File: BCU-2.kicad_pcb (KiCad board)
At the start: 2 copper layers, 106 x 91.4 mm, 92 parts, among them J1 Screw_Terminal_01x04, J2 Conn_01x12_Male, J3 Screw_Terminal_01x04, J4 Conn_01x05_Male, J5 Conn_01x05_Male, J6 Conn_01x04_Male, J7 Conn_01x04_Male, Q1 2N7002, Q2 NTF6P02, Q3 2N7002, Q4 2N7002, Q5 NTF6P02, Q6 2N7002, U1 Teensy3.2, U10 74LV1T08, U11 74LV1T08, U12 INA219xID, U13 INA219xID, U2 HCPL-181, U3 HCPL-181, U4 HCPL-181, U5 HCPL-181, U6 HCPL-181, U7 HCPL-181, U8 74LV1T08, U9 74LV1T08

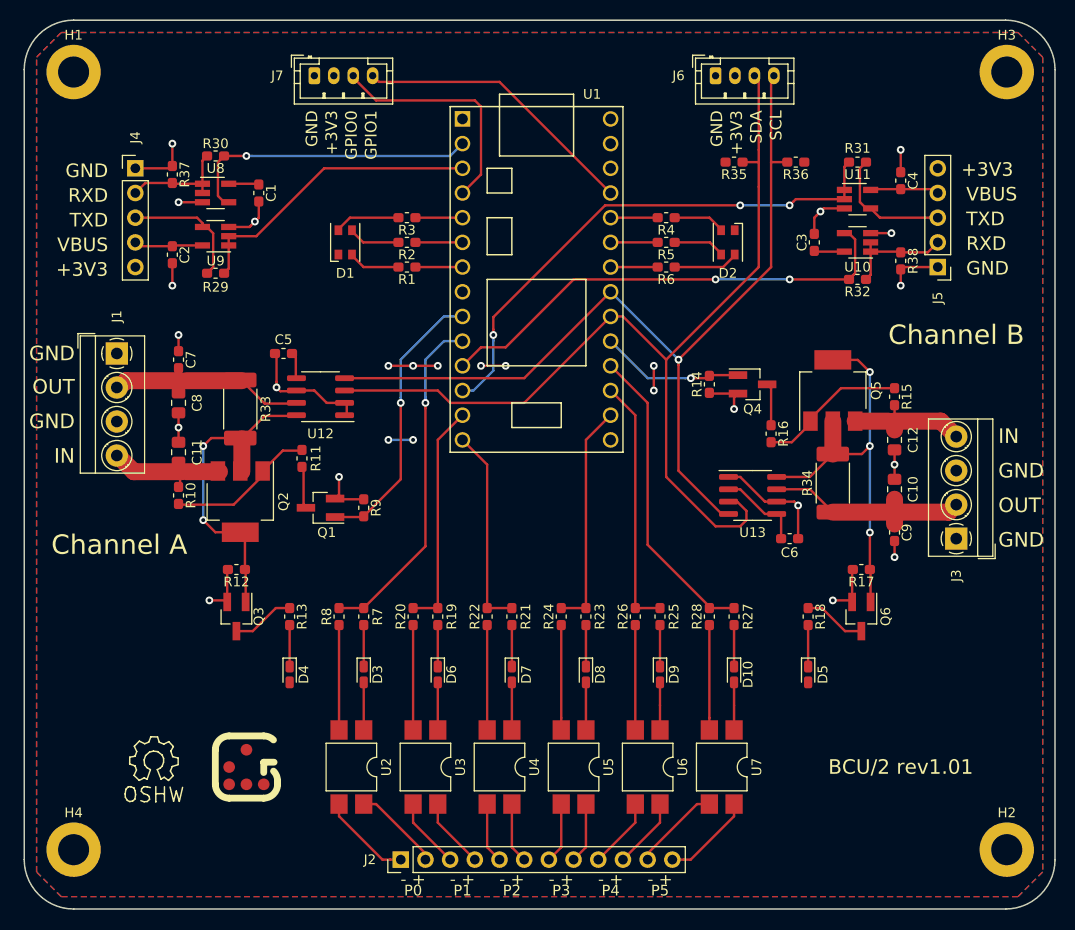
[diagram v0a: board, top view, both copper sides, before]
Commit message: PCB: Update layout for schematic changes
Signed-off-by: Geert Uytterhoeven <geert@linux-m68k.org>
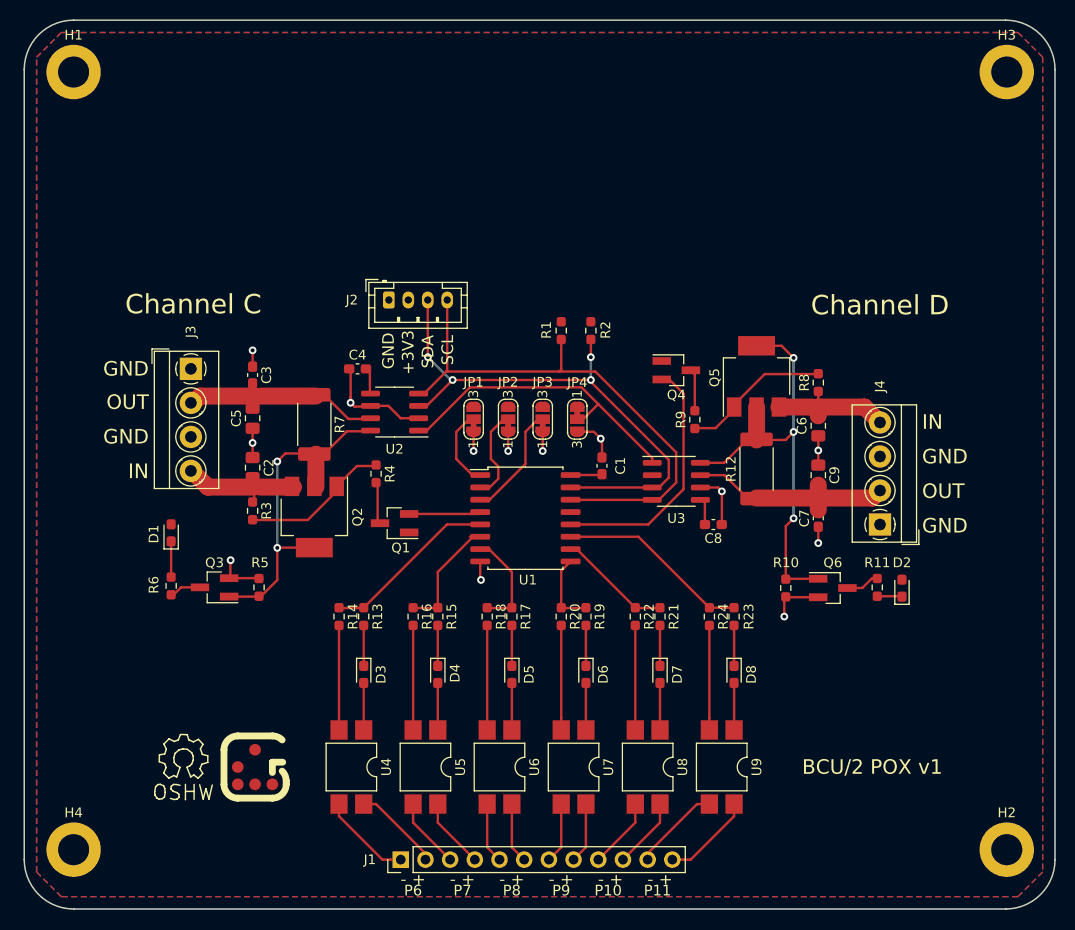
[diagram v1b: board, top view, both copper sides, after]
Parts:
- removed the C2 at (121.3, 66.7)
- removed the C3 at (187.3, 65.4)
- removed the C4 at (196.2, 59.1)
- removed the D1 at (139.1, 65.4)
- removed the D2 at (178.4, 65.4)
- removed the J4 at (117.5, 57.8)
- removed J5: Conn_01x05_Male, Connector_PinHeader_2.54mm:PinHeader_1x05_P2.54mm_Vertical
- removed J7: Conn_01x04_Male, Connector_JST:JST_PH_B4B-PH-K_1x04_P2.00mm_Vertical
- removed the R14 at (176.5, 80.0)
- removed R29, R30, R31, R32: 0*, Resistor_SMD:R_0603_1608Metric_Pad1.05x0.95mm_HandSolder
- removed the R3 at (145.4, 62.9)
- removed R35, R36: 4K7, Resistor_SMD:R_0603_1608Metric_Pad1.05x0.95mm_HandSolder
- removed R37, R38: 47K, Resistor_SMD:R_0603_1608Metric_Pad1.05x0.95mm_HandSolder
- removed the R4 at (172.1, 62.9)
- removed the R5 at (172.1, 65.4)
- removed the R6 at (172.1, 67.9)
- removed the R9 at (141.0, 92.7)
- removed U10, U11: 74LV1T08, Package_TO_SOT_SMD:SOT-23-5_HandSoldering
- removed the U8 at (125.7, 60.3)
- removed the U9 at (125.7, 64.8)
- added JP1: SolderJumper_3_Bridged12, Jumper:SolderJumper-3_P1.3mm_Bridged12_RoundedPad1.0x1.5mm_NumberLabels, F.Cu at (152.3, 83.6)
- added JP2: SolderJumper_3_Bridged12, Jumper:SolderJumper-3_P1.3mm_Bridged12_RoundedPad1.0x1.5mm_NumberLabels, F.Cu at (155.8, 83.6)
- added JP3: SolderJumper_3_Bridged12, Jumper:SolderJumper-3_P1.3mm_Bridged12_RoundedPad1.0x1.5mm_NumberLabels, F.Cu at (159.4, 83.6)
- added JP4: SolderJumper_3_Bridged12, Jumper:SolderJumper-3_P1.3mm_Bridged12_RoundedPad1.0x1.5mm_NumberLabels, F.Cu at (162.9, 83.6)
- C1: footprint Capacitor_SMD:C_0603_1608Metric_Pad1.05x0.95mm_HandSolder -> Capacitor_SMD:C_0603_1608Metric_Pad1.08x0.95mm_HandSolder
- C2: renamed from C11; footprint Capacitor_SMD:C_0805_2012Metric_Pad1.15x1.40mm_HandSolder -> Capacitor_SMD:C_0805_2012Metric_Pad1.18x1.45mm_HandSolder
- C3: renamed from C7; footprint Capacitor_SMD:C_0603_1608Metric_Pad1.05x0.95mm_HandSolder -> Capacitor_SMD:C_0603_1608Metric_Pad1.08x0.95mm_HandSolder
- C4: renamed from C5; footprint Capacitor_SMD:C_0603_1608Metric_Pad1.05x0.95mm_HandSolder -> Capacitor_SMD:C_0603_1608Metric_Pad1.08x0.95mm_HandSolder
- C5: renamed from C8; footprint Capacitor_SMD:C_0805_2012Metric_Pad1.15x1.40mm_HandSolder -> Capacitor_SMD:C_0805_2012Metric_Pad1.18x1.45mm_HandSolder
- C6: renamed from C12; footprint Capacitor_SMD:C_0805_2012Metric_Pad1.15x1.40mm_HandSolder -> Capacitor_SMD:C_0805_2012Metric_Pad1.18x1.45mm_HandSolder
- C7: renamed from C9; footprint Capacitor_SMD:C_0603_1608Metric_Pad1.05x0.95mm_HandSolder -> Capacitor_SMD:C_0603_1608Metric_Pad1.08x0.95mm_HandSolder
- C8: renamed from C6; footprint Capacitor_SMD:C_0603_1608Metric_Pad1.05x0.95mm_HandSolder -> Capacitor_SMD:C_0603_1608Metric_Pad1.08x0.95mm_HandSolder
- C9: renamed from C10; footprint Capacitor_SMD:C_0805_2012Metric_Pad1.15x1.40mm_HandSolder -> Capacitor_SMD:C_0805_2012Metric_Pad1.18x1.45mm_HandSolder
- D1: renamed from D4; footprint LED_SMD:LED_0603_1608Metric_Castellated -> LED_SMD:LED_0603_1608Metric_Pad1.05x0.95mm_HandSolder
- D2: renamed from D5; footprint LED_SMD:LED_0603_1608Metric_Castellated -> LED_SMD:LED_0603_1608Metric_Pad1.05x0.95mm_HandSolder
- D3: footprint LED_SMD:LED_0603_1608Metric_Castellated -> LED_SMD:LED_0603_1608Metric_Pad1.05x0.95mm_HandSolder
- D4: renamed from D6; footprint LED_SMD:LED_0603_1608Metric_Castellated -> LED_SMD:LED_0603_1608Metric_Pad1.05x0.95mm_HandSolder
- D5: renamed from D7; footprint LED_SMD:LED_0603_1608Metric_Castellated -> LED_SMD:LED_0603_1608Metric_Pad1.05x0.95mm_HandSolder
- D6: renamed from D8; footprint LED_SMD:LED_0603_1608Metric_Castellated -> LED_SMD:LED_0603_1608Metric_Pad1.05x0.95mm_HandSolder
- D7: renamed from D9; footprint LED_SMD:LED_0603_1608Metric_Castellated -> LED_SMD:LED_0603_1608Metric_Pad1.05x0.95mm_HandSolder
- D8: renamed from D10; footprint LED_SMD:LED_0603_1608Metric_Castellated -> LED_SMD:LED_0603_1608Metric_Pad1.05x0.95mm_HandSolder
- R1: value 680 -> 4K7; footprint Resistor_SMD:R_0603_1608Metric_Pad1.05x0.95mm_HandSolder -> Resistor_SMD:R_0603_1608Metric_Pad0.98x0.95mm_HandSolder
- R10: renamed from R17; footprint Resistor_SMD:R_0603_1608Metric_Pad1.05x0.95mm_HandSolder -> Resistor_SMD:R_0603_1608Metric_Pad0.98x0.95mm_HandSolder
- R11: renamed from R18; footprint Resistor_SMD:R_0603_1608Metric_Pad1.05x0.95mm_HandSolder -> Resistor_SMD:R_0603_1608Metric_Pad0.98x0.95mm_HandSolder
- R12: renamed from R34; footprint Resistor_SMD:R_2512_6332Metric_Pad1.52x3.35mm_HandSolder -> Resistor_SMD:R_2512_6332Metric_Pad1.40x3.35mm_HandSolder
- R13: renamed from R7; footprint Resistor_SMD:R_0603_1608Metric_Pad1.05x0.95mm_HandSolder -> Resistor_SMD:R_0603_1608Metric_Pad0.98x0.95mm_HandSolder
- R14: renamed from R8; footprint Resistor_SMD:R_0603_1608Metric_Pad1.05x0.95mm_HandSolder -> Resistor_SMD:R_0603_1608Metric_Pad0.98x0.95mm_HandSolder
- R15: renamed from R19; footprint Resistor_SMD:R_0603_1608Metric_Pad1.05x0.95mm_HandSolder -> Resistor_SMD:R_0603_1608Metric_Pad0.98x0.95mm_HandSolder
- R16: renamed from R20; footprint Resistor_SMD:R_0603_1608Metric_Pad1.05x0.95mm_HandSolder -> Resistor_SMD:R_0603_1608Metric_Pad0.98x0.95mm_HandSolder
- R17: renamed from R21; footprint Resistor_SMD:R_0603_1608Metric_Pad1.05x0.95mm_HandSolder -> Resistor_SMD:R_0603_1608Metric_Pad0.98x0.95mm_HandSolder
- R18: renamed from R22; footprint Resistor_SMD:R_0603_1608Metric_Pad1.05x0.95mm_HandSolder -> Resistor_SMD:R_0603_1608Metric_Pad0.98x0.95mm_HandSolder
- R19: renamed from R23; footprint Resistor_SMD:R_0603_1608Metric_Pad1.05x0.95mm_HandSolder -> Resistor_SMD:R_0603_1608Metric_Pad0.98x0.95mm_HandSolder
- R2: value 100 -> 4K7; footprint Resistor_SMD:R_0603_1608Metric_Pad1.05x0.95mm_HandSolder -> Resistor_SMD:R_0603_1608Metric_Pad0.98x0.95mm_HandSolder
- R20: renamed from R24; footprint Resistor_SMD:R_0603_1608Metric_Pad1.05x0.95mm_HandSolder -> Resistor_SMD:R_0603_1608Metric_Pad0.98x0.95mm_HandSolder
- R21: renamed from R25; footprint Resistor_SMD:R_0603_1608Metric_Pad1.05x0.95mm_HandSolder -> Resistor_SMD:R_0603_1608Metric_Pad0.98x0.95mm_HandSolder
- R22: renamed from R26; footprint Resistor_SMD:R_0603_1608Metric_Pad1.05x0.95mm_HandSolder -> Resistor_SMD:R_0603_1608Metric_Pad0.98x0.95mm_HandSolder
- R23: renamed from R27; footprint Resistor_SMD:R_0603_1608Metric_Pad1.05x0.95mm_HandSolder -> Resistor_SMD:R_0603_1608Metric_Pad0.98x0.95mm_HandSolder
- R24: renamed from R28; footprint Resistor_SMD:R_0603_1608Metric_Pad1.05x0.95mm_HandSolder -> Resistor_SMD:R_0603_1608Metric_Pad0.98x0.95mm_HandSolder
- R3: renamed from R10; footprint Resistor_SMD:R_0603_1608Metric_Pad1.05x0.95mm_HandSolder -> Resistor_SMD:R_0603_1608Metric_Pad0.98x0.95mm_HandSolder
- R4: renamed from R11; footprint Resistor_SMD:R_0603_1608Metric_Pad1.05x0.95mm_HandSolder -> Resistor_SMD:R_0603_1608Metric_Pad0.98x0.95mm_HandSolder
- R5: renamed from R12; footprint Resistor_SMD:R_0603_1608Metric_Pad1.05x0.95mm_HandSolder -> Resistor_SMD:R_0603_1608Metric_Pad0.98x0.95mm_HandSolder
- R6: renamed from R13; footprint Resistor_SMD:R_0603_1608Metric_Pad1.05x0.95mm_HandSolder -> Resistor_SMD:R_0603_1608Metric_Pad0.98x0.95mm_HandSolder
- R7: renamed from R33; footprint Resistor_SMD:R_2512_6332Metric_Pad1.52x3.35mm_HandSolder -> Resistor_SMD:R_2512_6332Metric_Pad1.40x3.35mm_HandSolder
- R8: renamed from R15; footprint Resistor_SMD:R_0603_1608Metric_Pad1.05x0.95mm_HandSolder -> Resistor_SMD:R_0603_1608Metric_Pad0.98x0.95mm_HandSolder
- R9: renamed from R16; footprint Resistor_SMD:R_0603_1608Metric_Pad1.05x0.95mm_HandSolder -> Resistor_SMD:R_0603_1608Metric_Pad0.98x0.95mm_HandSolder
- U1: value Teensy3.2 -> PCF8574; footprint teensy:Teensy32-DIP28 -> Package_SO:SOIC-16W_7.5x10.3mm_P1.27mm
- moved C1 45.1 mm to (165.5, 88.4)
- moved J2 40.8 mm to (143.6, 71.3)
- moved U1 24.6 mm to (157.6, 93.8), turned to 0 degrees
- moved R2 21.0 mm to (164.3, 74.5), turned to -90 degrees
- moved D1 19.0 mm to (121.2, 95.3), turned to 90 degrees
- moved R1 17.2 mm to (161.3, 74.5), turned to -90 degrees
- moved D2 13.1 mm to (196.3, 101.0), turned to 90 degrees
- moved R6 12.6 mm to (121.2, 100.7), turned to -90 degrees
- moved R10 8.00 mm to (184.4, 101.0), turned to -90 degrees
- moved C7 7.98 mm to (187.7, 93.8)
- moved C8 7.98 mm to (176.9, 94.4)
- moved C9 7.98 mm to (187.7, 89.4)
- moved J4 7.98 mm to (194.1, 94.4)
- moved Q4 7.98 mm to (173.1, 78.6)
- moved Q5 7.98 mm to (181.4, 79.2)
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- renumbered J2 to J1, J6 to J2, J1 to J3, J3 to J4, U12 to U2, U13 to U3, U2 to U4, U3 to U5, U4 to U6, U5 to U7, U6 to U8, U7 to U9
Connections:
- net /Power Channel A/IN renamed /Power Channel C/IN
- net /Power Channel A/OUT renamed /Power Channel C/OUT
- net /Power Channel B/IN renamed /Power Channel D/IN
- net /Power Channel B/OUT renamed /Power Channel D/OUT
- net P0+ renamed P6+
- net P0- renamed P6-
- net P1+ renamed P7+
- net P1- renamed P7-
- net P2+ renamed P8+
- net P2- renamed P8-
- net P3+ renamed P9+
- net P3- renamed P9-
- net P4+ renamed P10+
- net P4- renamed P10-
- net P5+ renamed P11+
- net P5- renamed P11-
- C1 pad 1: GND -> +3V3
- C1 pad 2: +3V3 -> GND
- Q1 pad 1: PWRA_EN -> +3V3
- Q1 pad 2: GND -> PWRC_EN
- Q4 pad 1: PWRB_EN -> +3V3
- Q4 pad 2: GND -> PWRD_EN
- R1 pad 1: LEDA_R -> +3V3
- R1 pad 2: Net-(D1-Pad2) -> SCL
- R13 pad 1: P0 -> P6
- R14 pad 1: P0 -> P6
- R15 pad 1: P1 -> P7
- R16 pad 1: P1 -> P7
- R17 pad 1: P2 -> P8
- R18 pad 1: P2 -> P8
- R19 pad 1: P3 -> P9
- R2 pad 1: LEDA_G -> +3V3
- R2 pad 2: Net-(D1-Pad3) -> SDA
- R20 pad 1: P3 -> P9
- R21 pad 1: P4 -> P10
- R22 pad 1: P4 -> P10
- R23 pad 1: P5 -> P11
- R24 pad 1: P5 -> P11
- U1 pad 1: GND -> Net-(JP1-Pad2)
- U1 pad 10: P0 -> P10
- U1 pad 11: UARTB_RX -> P11
- U1 pad 12: UARTB_TX -> PWRD_EN
- U1 pad 13: P1 -> unconnected-(U1-Pad13)
- U1 pad 14: P2 -> SCL
- U1 pad 2: UARTA_RX -> Net-(JP2-Pad2)
- U1 pad 3: UARTA_TX -> Net-(JP3-Pad2)
- U1 pad 4: GPIO0 -> PWRC_EN
- U1 pad 5: LEDA_B -> P6
- U1 pad 6: LEDA_G -> P7
- U1 pad 7: LEDA_R -> P8
- U1 pad 8: (no net) -> GND
- U1 pad 9: PWRA_EN -> P9
- U2 pad 1: GND -> /Power Channel C/A1
- U3 pad 1: GND -> /Power Channel C/A1
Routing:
- net UARTB_TX: track 54.7 -> 0.00 mm, vias 3 -> 0
- net UARTB_RX: track 49.2 -> 0.00 mm, vias 2 -> 0
- net GND: track 96.2 -> 49.2 mm, vias 25 -> 13
- net SDA: track 99.8 -> 55.6 mm, vias 0 -> 4
- net SCL: track 93.4 -> 55.7 mm, vias 1 -> 0
- net P0: track 35.3 -> 0.00 mm, vias 1 -> 0
- net /Power Channel C/A1: track 0.00 -> 32.2 mm
- net P5: track 31.7 -> 0.00 mm
- net UARTA_TX: track 31.0 -> 0.00 mm
- net UARTA_RX: track 30.8 -> 0.00 mm, vias 1 -> 0
- net GPIO1: track 29.5 -> 0.00 mm
- net PWRA_EN: track 28.9 -> 0.00 mm, vias 1 -> 0
- net P4: track 26.0 -> 0.00 mm
- net PWRD_EN: track 0.00 -> 25.8 mm
- net GPIO0: track 24.3 -> 0.00 mm
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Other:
- board text added: "BCU/2 POX v1"
- board text added: "Channel C"
- board text added: "Channel D"
- board text added: "P10"
- board text added: "P11"
- board text added: "P6"
- board text added: "P7"
- board text added: "P8"
- board text added: "P9"
- board text removed: "BCU/2 rev1.01"
- board text removed: "Channel A"
- board text removed: "Channel B"
- board text removed: "GPIO0"
- board text removed: "GPIO1"
- board text removed: "P0"
- board text removed: "P1"
- board text removed: "P2"
- board text removed: "P3"
- board text removed: "P4"
- board text removed: "P5"
- board text removed: "RXD"
- board text removed: "TXD"
- board text removed: "VBUS"

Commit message: PCB: Update size and mounting holes
Signed-off-by: Geert Uytterhoeven <geert@linux-m68k.org>
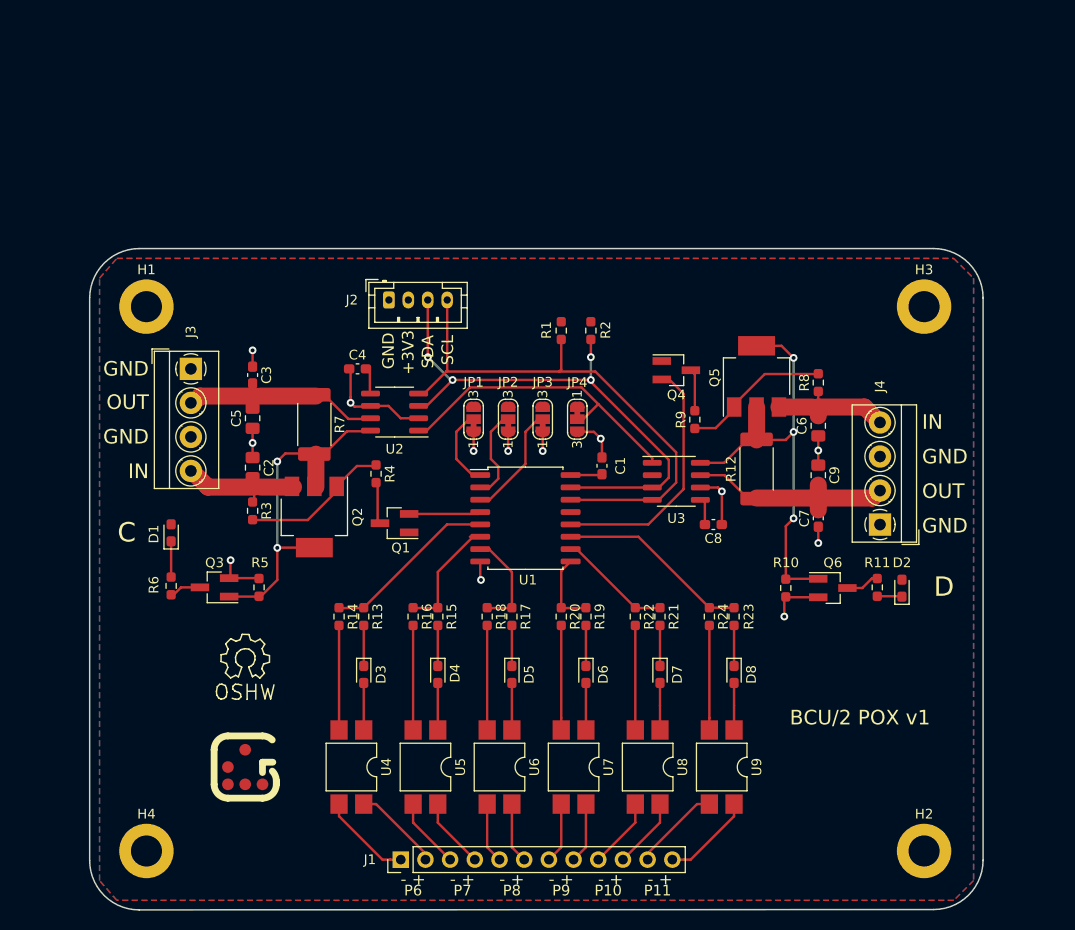
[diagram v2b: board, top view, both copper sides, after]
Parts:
- moved H3 25.6 mm to (198.6, 72.0)
- moved H1 25.3 mm to (118.6, 72.0)
- moved OSHW 12.1 mm to (128.8, 108.2)
- moved H2 8.51 mm to (198.6, 128.0)
- moved H4 7.49 mm to (118.6, 128.0)
- moved Glider 1.02 mm to (128.8, 119.4)
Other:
- board size 106 x 91.4 mm -> 91.9 x 68 mm
- board text added: "C"
- board text added: "D"
- board text removed: "Channel C"
- board text removed: "Channel D"
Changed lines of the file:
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@@
   )
   (footprint "Symbols:Symbol_OSHW-Logo_SilkScreen" (layer "F.Cu")
-    (at 122.428 118.51005)
+    (at 128.778 108.204)
     (descr "Symbol, OSHW-Logo, Silk Screen,")
     (tags "Symbol, OSHW-Logo, Silk Screen,")
@@
     )
   )
-  (footprint "MountingHole:MountingHole_3.2mm_M3_DIN965_Pad" (layer "F.Cu")
-    (at 207.125 127.88)
+  (footprint "MountingHole:MountingHole_3.2mm_M3_DIN965_Pad" locked (layer "F.Cu")
+    (at 198.618 128.016)
     (descr "Mounting Hole 3.2mm, M3, DIN965")
     (tags "mounting hole 3.2mm m3 din965")
@@
     (fp_circle (center 0 0) (end 2.8 0) (layer "Cmts.User") (width 0.15) (fill none))
     (fp_circle (center 0 0) (end 3.05 0) (layer "F.CrtYd") (width 0.05) (fill none))
-    (pad "1" thru_hole circle (at 0 0) (size 5.6 5.6) (drill 3.2) (layers *.Cu *.Mask)
+    (pad "1" thru_hole circle locked (at 0 0) (size 5.6 5.6) (drill 3.2) (layers *.Cu *.Mask)
       (net 1 "GND") (pinfunction "1") (pintype "input"))
   )
-  (footprint "MountingHole:MountingHole_3.2mm_M3_DIN965_Pad" (layer "F.Cu")
-    (at 207.125 47.88)
+  (footprint "MountingHole:MountingHole_3.2mm_M3_DIN965_Pad" locked (layer "F.Cu")
+    (at 198.618 72.016)
     (descr "Mounting Hole 3.2mm, M3, DIN965")
     (tags "mounting hole 3.2mm m3 din965")
@@
     (fp_circle (center 0 0) (end 2.8 0) (layer "Cmts.User") (width 0.15) (fill none))
     (fp_circle (center 0 0) (end 3.05 0) (layer "F.CrtYd") (width 0.05) (fill none))
-    (pad "1" thru_hole circle (at 0 0) (size 5.6 5.6) (drill 3.2) (layers *.Cu *.Mask)
+    (pad "1" thru_hole circle locked (at 0 0) (size 5.6 5.6) (drill 3.2) (layers *.Cu *.Mask)
       (net 1 "GND") (pinfunction "1") (pintype "input"))
   )
-  (footprint "MountingHole:MountingHole_3.2mm_M3_DIN965_Pad" (layer "F.Cu")
-    (at 111.125 127.88)
+  (footprint "MountingHole:MountingHole_3.2mm_M3_DIN965_Pad" locked (layer "F.Cu")
+    (at 118.618 128.016)
     (descr "Mounting Hole 3.2mm, M3, DIN965")
     (tags "mounting hole 3.2mm m3 din965")
@@
     (fp_circle (center 0 0) (end 2.8 0) (layer "Cmts.User") (width 0.15) (fill none))
     (fp_circle (center 0 0) (end 3.05 0) (layer "F.CrtYd") (width 0.05) (fill none))
-    (pad "1" thru_hole circle (at 0 0) (size 5.6 5.6) (drill 3.2) (layers *.Cu *.Mask)
+    (pad "1" thru_hole circle locked (at 0 0) (size 5.6 5.6) (drill 3.2) (layers *.Cu *.Mask)
       (net 1 "GND") (pinfunction "1") (pintype "input"))
   )
-  (footprint "MountingHole:MountingHole_3.2mm_M3_DIN965_Pad" (layer "F.Cu")
-    (at 111.125 47.88)
+  (footprint "MountingHole:MountingHole_3.2mm_M3_DIN965_Pad" locked (layer "F.Cu")
+    (at 118.618 72.016)
     (descr "Mounting Hole 3.2mm, M3, DIN965")
     (tags "mounting hole 3.2mm m3 din965")
@@
     (fp_circle (center 0 0) (end 2.8 0) (layer "Cmts.User") (width 0.15) (fill none))
     (fp_circle (center 0 0) (end 3.05 0) (layer "F.CrtYd") (width 0.05) (fill none))
-    (pad "1" thru_hole circle (at 0 0) (size 5.6 5.6) (drill 3.2) (layers *.Cu *.Mask)
+    (pad "1" thru_hole circle locked (at 0 0) (size 5.6 5.6) (drill 3.2) (layers *.Cu *.Mask)
       (net 1 "GND") (pinfunction "1") (pintype "input"))
   )
@@
   )
   (footprint "geert:Glider_bvba_G_Medium" (layer "F.Cu")
-    (at 129.794 119.38)
+    (at 128.778 119.38)
     (attr through_hole board_only exclude_from_bom)
     (fp_text reference "Glider" (at 0 0.5) (layer "F.SilkS") hide
@@
       ))
   )
-  (gr_line (start 212.09 128.905) (end 212.09 47.625) (layer "Edge.Cuts") (width 0.15))
-  (gr_arc (start 111.125 133.985) (mid 107.532898 132.497102) (end 106.045 128.905) (layer "Edge.Cuts") (width 0.15))
-  (gr_arc (start 212.09 128.905) (mid 210.602102 132.497102) (end 207.01 133.985) (layer "Edge.Cuts") (width 0.15))
-  (gr_line (start 111.125 42.545) (end 207.01 42.545) (layer "Edge.Cuts") (width 0.15))
-  (gr_line (start 111.125 133.985) (end 207.01 133.985) (layer "Edge.Cuts") (width 0.15))
-  (gr_arc (start 106.045 47.625) (mid 107.532898 44.032898) (end 111.125 42.545) (layer "Edge.Cuts") (width 0.15))
-  (gr_line (start 106.045 47.625) (end 106.045 128.905) (layer "Edge.Cuts") (width 0.15))
-  (gr_arc (start 207.01 42.545) (mid 210.602102 44.032898) (end 212.09 47.625) (layer "Edge.Cuts") (width 0.15))
+  (gr_line (start 204.687898 128.959796) (end 204.687898 71.12) (layer "Edge.Cuts") (width 0.15))
+  (gr_arc (start 117.855998 134.075898) (mid 114.263896 132.588) (end 112.775998 128.995898) (layer "Edge.Cuts") (width 0.15))
+  (gr_arc (start 204.687898 128.959796) (mid 203.2 132.551898) (end 199.607898 134.039796) (layer "Edge.Cuts") (width 0.15))
+  (gr_line (start 117.856 66.04) (end 199.607898 66.04) (layer "Edge.Cuts") (width 0.15))
+  (gr_line (start 117.855998 134.075898) (end 199.607898 134.039796) (layer "Edge.Cuts") (width 0.15))
+  (gr_arc (start 112.776 71.083898) (mid 114.287069 67.525654) (end 117.856 66.04) (layer "Edge.Cuts") (width 0.15))
+  (gr_line (start 112.776 71.083898) (end 112.775998 128.995898) (layer "Edge.Cuts") (width 0.15))
+  (gr_arc (start 199.607898 66.04) (mid 203.2 67.527898) (end 204.687898 71.12) (layer "Edge.Cuts") (width 0.15))
   (gr_text "IN\n" (at 118.872 88.95875) (layer "F.SilkS")
     (effects (font (size 1.5 1.5) (thickness 0.3)) (justify right))
@@
     (effects (font (size 1.5 1.5) (thickness 0.3)) (justify right))
   )
-  (gr_text "Channel C" (at 123.444 71.78355) (layer "F.SilkS")
+  (gr_text "C" (at 116.586 95.25) (layer "F.SilkS")
     (effects (font (size 2 2) (thickness 0.4)))
   )
@@
     (effects (font (size 1.2 1.2) (thickness 0.2)) (justify right))
   )
-  (gr_text "BCU/2 POX v1" (at 193.294 119.38) (layer "F.SilkS")
+  (gr_text "BCU/2 POX v1" (at 192.024 114.3) (layer "F.SilkS")
     (effects (font (size 1.5 1.5) (thickness 0.3)))
   )
@@
     (effects (font (size 1.1 1.25) (thickness 0.15)))
   )
-  (gr_text "Channel D" (at 194.084 71.882) (layer "F.SilkS")
+  (gr_text "D" (at 200.66 100.838) (layer "F.SilkS")
     (effects (font (size 2 2) (thickness 0.4)))
   )
@@
     (polygon
       (pts
-        (xy 107.315 130.175)
-        (xy 107.315 46.355)
-        (xy 109.855 43.815)
-        (xy 208.28 43.815)
-        (xy 210.82 46.355)
-        (xy 210.82 130.175)
-        (xy 208.28 132.715)
-        (xy 109.855 132.715)
+        (xy 113.792 131.064)
+        (xy 113.792 69.088)
+        (xy 115.57 67.056)
+        (xy 201.676 67.056)
+        (xy 203.708 69.088)
+        (xy 203.708 131.064)
+        (xy 201.676 133.096)
+        (xy 115.57 133.096)
       )
     )
@@
     (polygon
       (pts
-        (xy 107.315 130.175)
-        (xy 107.315 46.355)
-        (xy 109.855 43.815)
-        (xy 208.28 43.815)
-        (xy 210.82 46.355)
-        (xy 210.82 130.175)
-        (xy 208.28 132.715)
-        (xy 109.855 132.715)
+        (xy 113.792 131.064)
+        (xy 113.792 69.088)
+        (xy 115.57 67.056)
+        (xy 201.676 67.056)
+        (xy 203.708 69.088)
+        (xy 203.708 131.064)
+        (xy 201.676 133.096)
+        (xy 115.57 133.096)
       )
     )
